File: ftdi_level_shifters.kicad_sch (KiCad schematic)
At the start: 9 parts, among them U32 NTB0104_DHVQFN, U45 NTB0104_DHVQFN, U46 NTB0104_DHVQFN

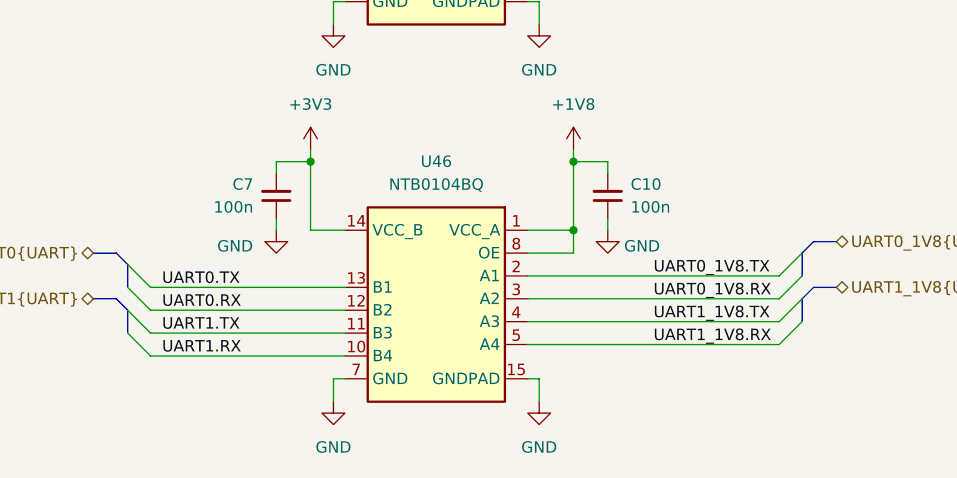
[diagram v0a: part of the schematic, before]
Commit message: [#84768] Add missing connections on sch
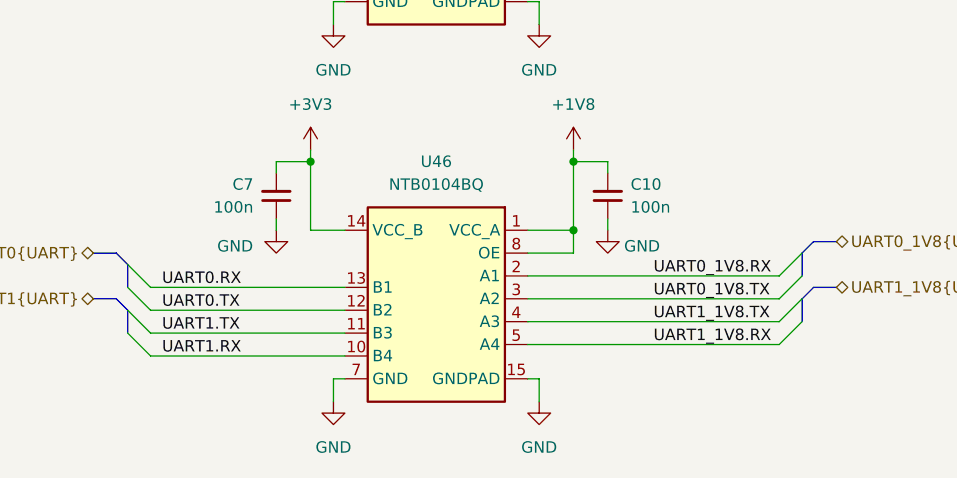
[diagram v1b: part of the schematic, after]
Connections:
- net UART0.RX: now also U46.13 (B1); no longer U46.12 (B2)
- net UART0.TX: now also U46.12 (B2); no longer U46.13 (B1)
- net UART0_1V8.RX: now also U46.2 (A1); no longer U46.3 (A2)
- net UART0_1V8.TX: now also U46.3 (A2); no longer U46.2 (A1)
